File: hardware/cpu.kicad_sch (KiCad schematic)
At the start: 8 parts, among them U1 H3

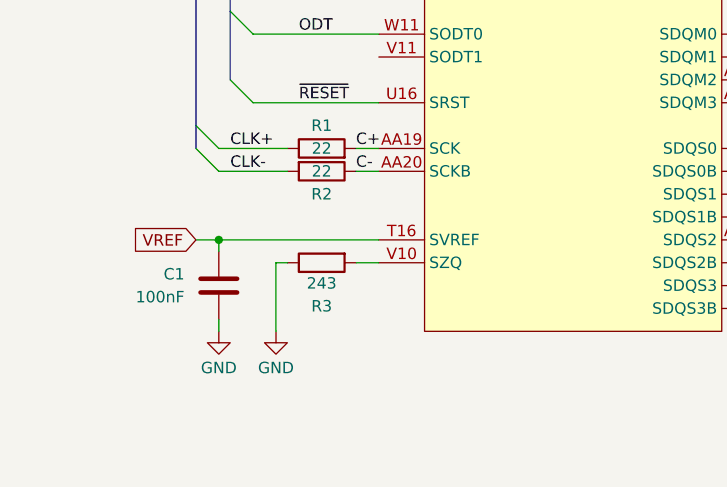
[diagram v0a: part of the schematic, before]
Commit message: Decoupled DDR3 and drew RJ45 connector
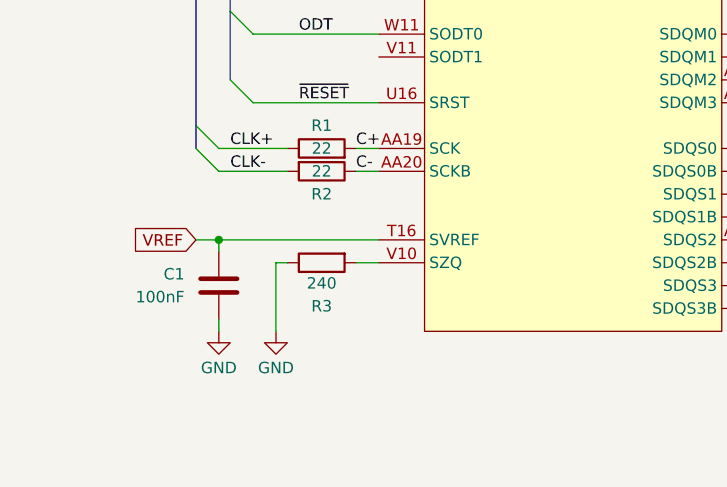
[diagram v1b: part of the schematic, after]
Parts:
- C1, C13, C14, C2: LCSC Part # (none) -> C1525
- R1, R2: LCSC Part # (none) -> C25092
- R3: value 243 -> 240; LCSC Part # (none) -> C23350
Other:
- company: (none) -> Icy Electronics
- title: (none) -> Icepi CM0
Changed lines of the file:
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@@
 	(generator_version "9.0")
 	(paper "A4")
+	(title_block
+		(title "Icepi CM0")
+		(date "2025-11-03")
+		(rev "v1.0")
+		(company "Icy Electronics")
+		(comment 1 "Chengyin Yao (cheyao)")
+		(comment 2 "https://github.com/cheyao/icepi-cm0")
+	)
 	(text "USB0 is OTG?"
 		(exclude_from_sim no)
@@
 			)
 		)
-		(property "LCSC Part #" ""
+		(property "LCSC Part #" "C25092"
 			(at 53.34 149.86 90)
 			(effects
@@
 			)
 		)
-		(property "Value" "243"
+		(property "Value" "240"
 			(at 53.34 164.846 90)
 			(effects
@@
 			)
 		)
-		(property "LCSC Part #" ""
+		(property "LCSC Part #" "C23350"
 			(at 53.34 162.56 90)
 			(effects
@@
 			)
 		)
-		(property "LCSC Part #" ""
+		(property "LCSC Part #" "C1525"
 			(at 41.91 165.1 0)
 			(effects
@@
 			)
 		)
+		(property "LCSC Part #" "C1525"
+			(at 204.47 27.94 0)
+			(effects
+				(font
+					(size 1.27 1.27)
+				)
+				(hide yes)
+			)
+		)
 		(pin "1"
 		)
@@
 			)
 		)
-		(property "LCSC Part #" ""
+		(property "LCSC Part #" "C25092"
 			(at 53.34 152.4 90)
 			(effects
@@
 			)
 		)
+		(property "LCSC Part #" "C1525"
+			(at 212.09 110.49 0)
+			(effects
+				(font
+					(size 1.27 1.27)
+				)
+				(hide yes)
+			)
+		)
 		(pin "1"
 		)
@@
 			(at 284.48 104.14 0)
 			(effects
+				(font
+					(size 1.27 1.27)
+				)
+				(hide yes)
+			)
+		)
+		(property "LCSC Part #" "C1525"
+			(at 284.48 104.14 0)
+			(effects
